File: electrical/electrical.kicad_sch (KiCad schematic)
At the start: 0 parts

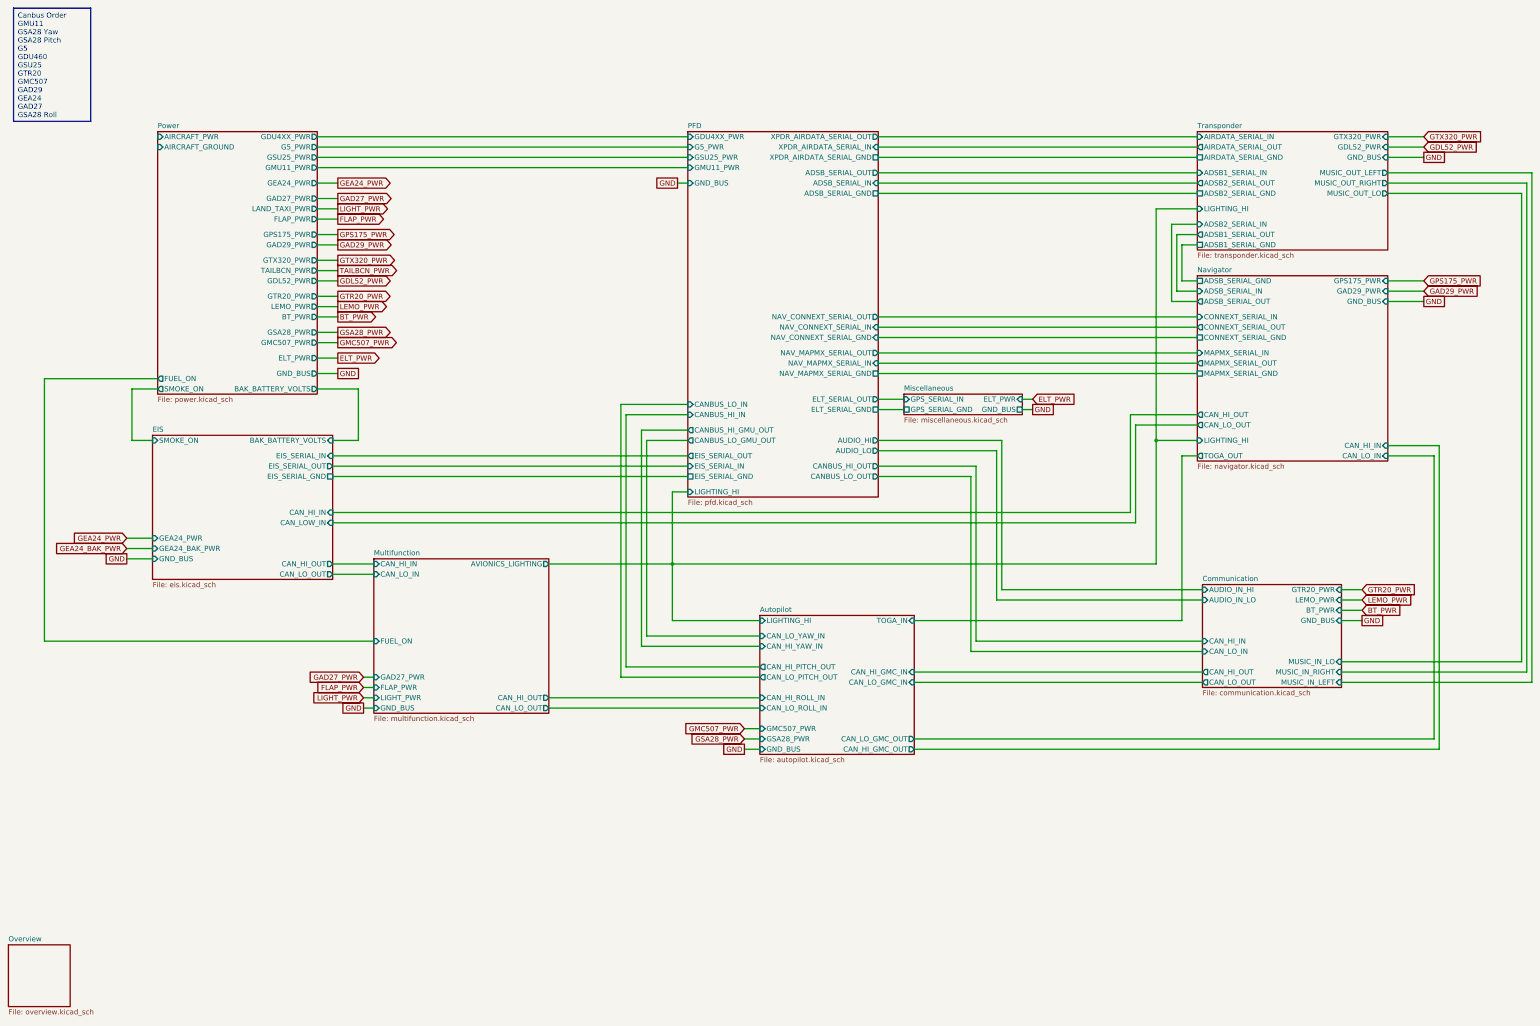
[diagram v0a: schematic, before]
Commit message: Added Altitude Encoder for 320, also added RS232 air data to Transponder in case upgrade to a GTX 327
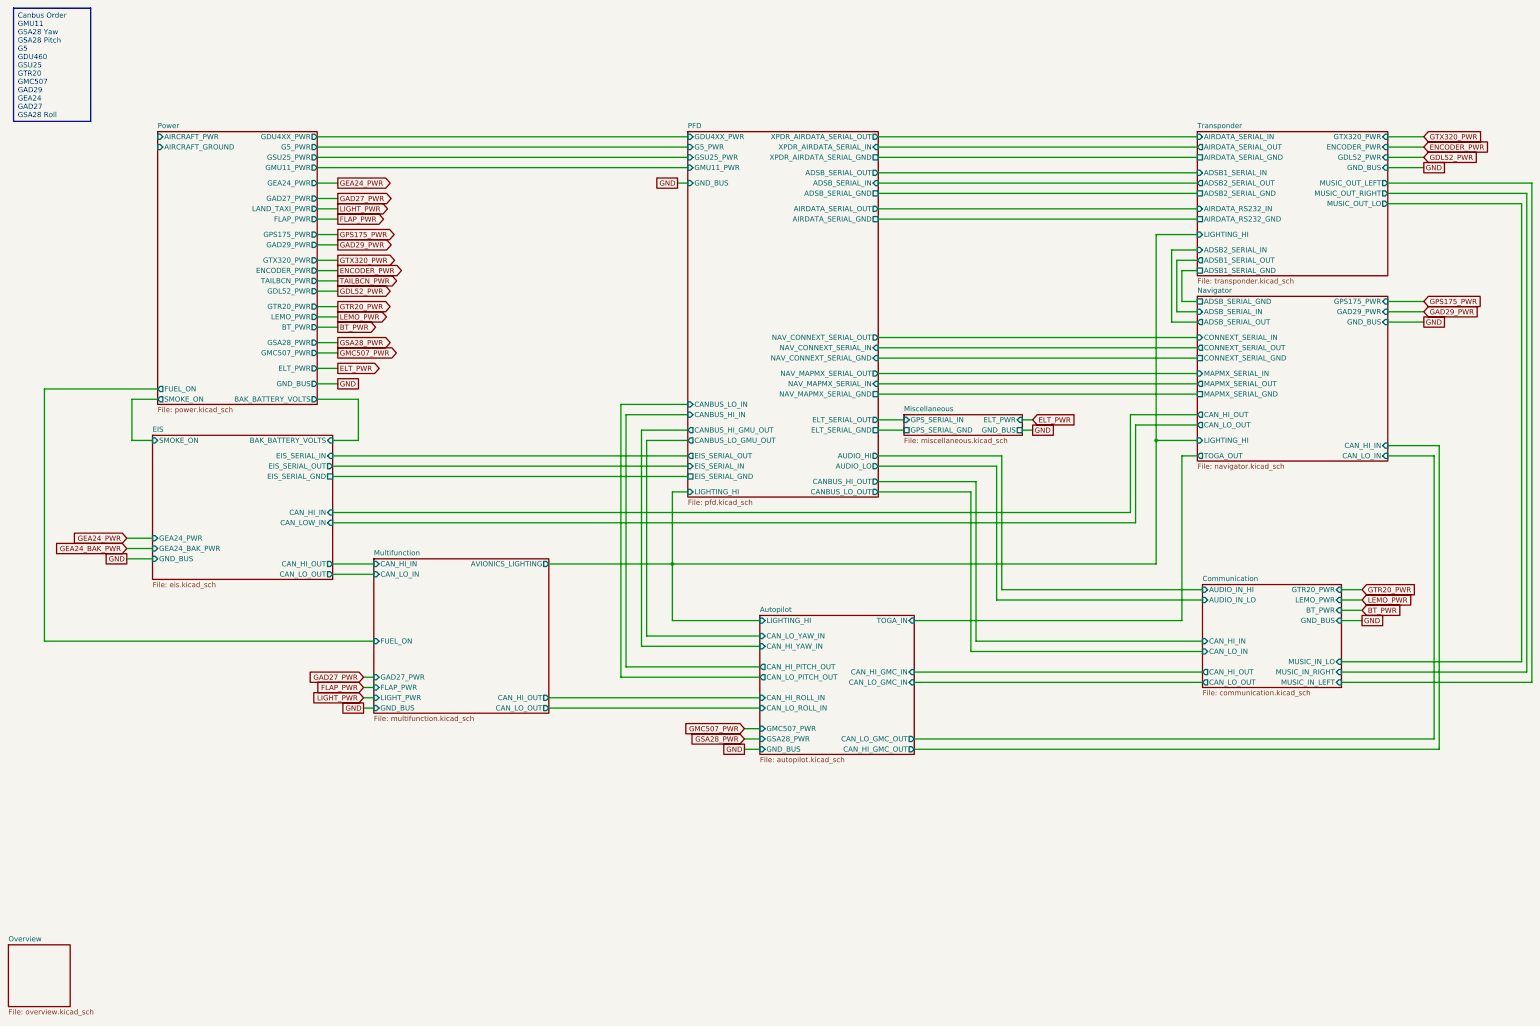
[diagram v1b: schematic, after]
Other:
- sheet PFD ports: added AIRDATA_SERIAL_GND, AIRDATA_SERIAL_OUT; removed none
- sheet Power ports: added ENCODER_PWR; removed none
- sheet Transponder ports: added AIRDATA_RS232_GND, AIRDATA_RS232_IN, ENCODER_PWR; removed none

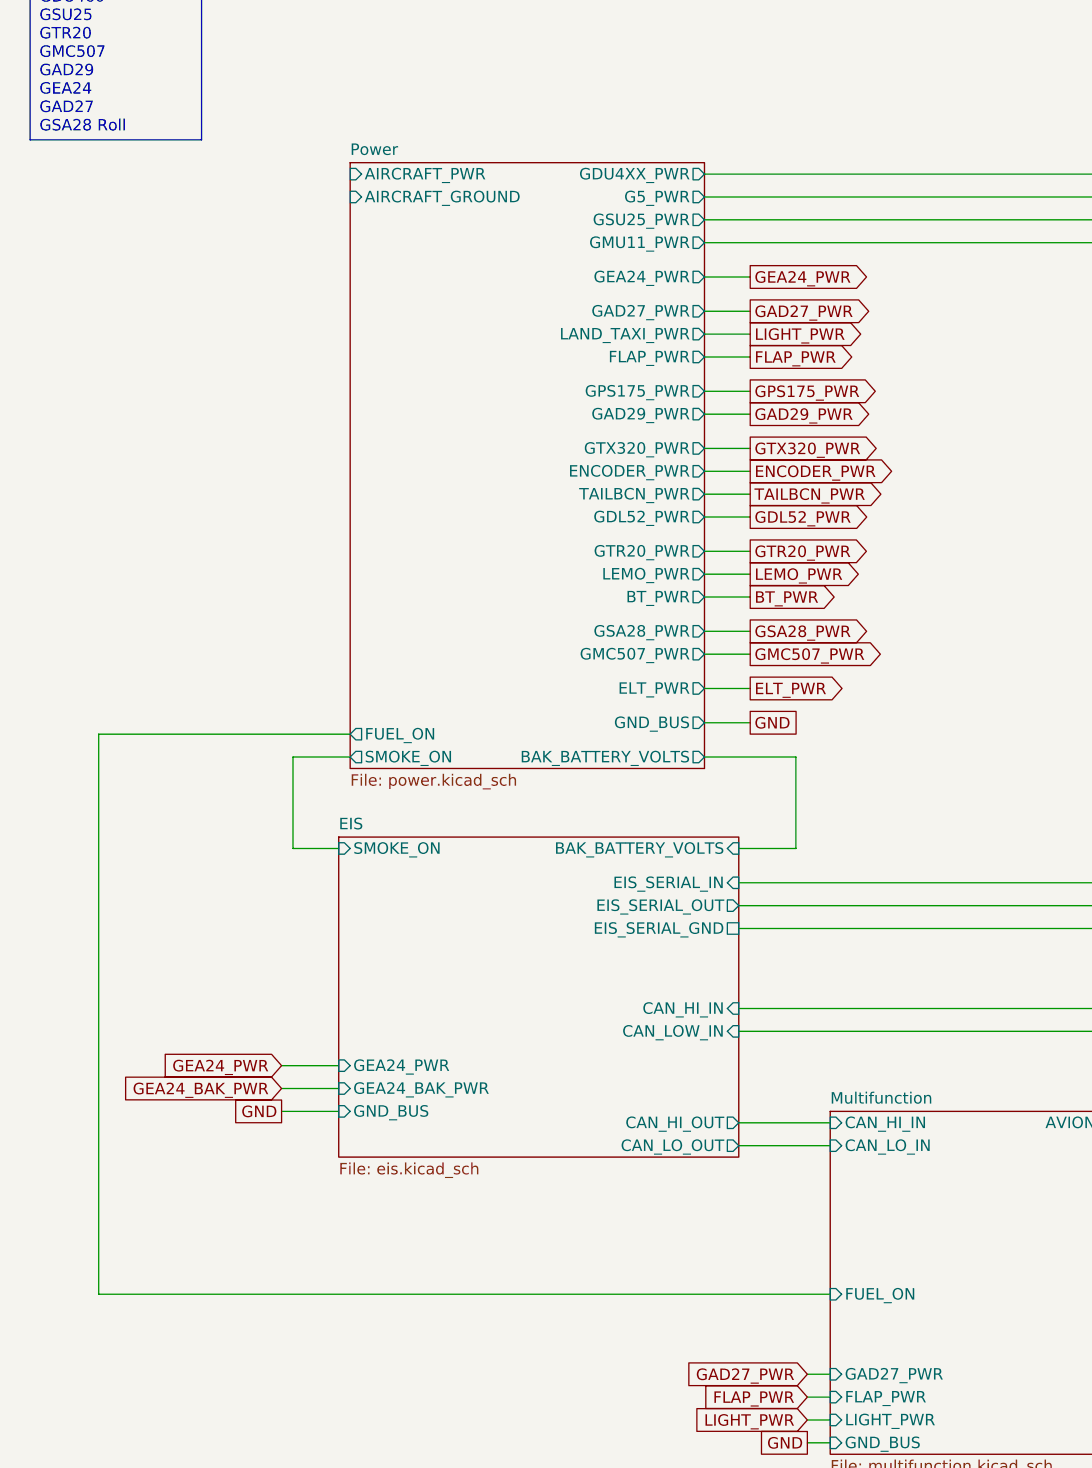
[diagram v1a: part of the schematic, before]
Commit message: Added AV breaker. Added diodes to TOGA. Moved smoke to use roll trim. Changec cabin & panel to use a single fuse.
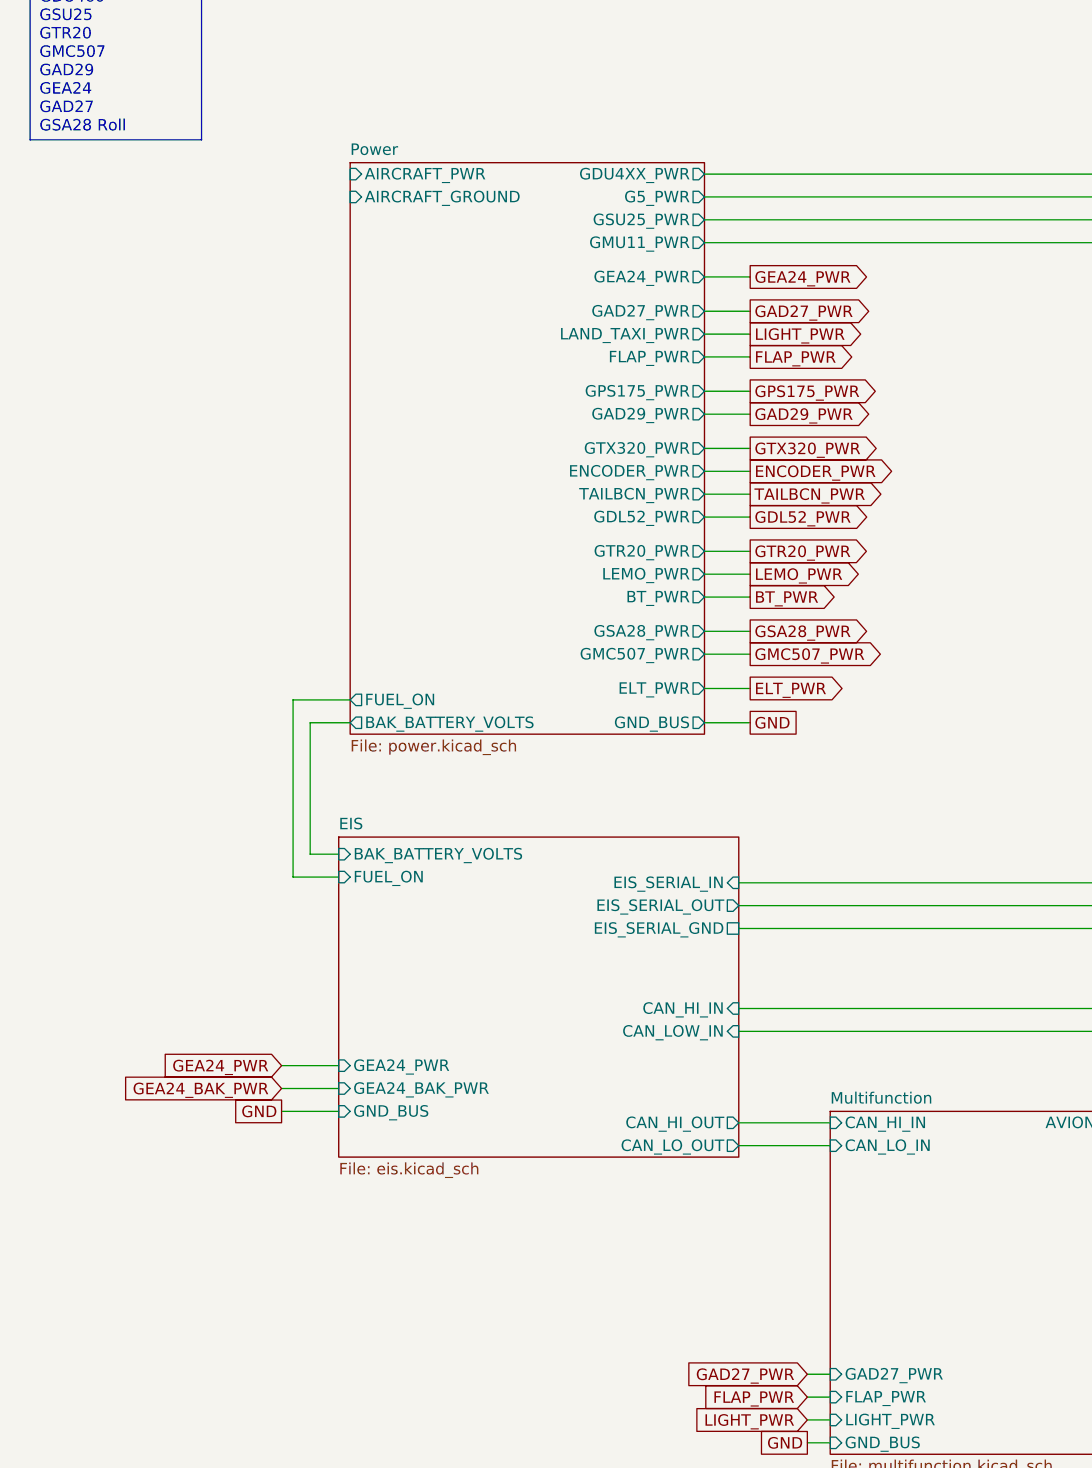
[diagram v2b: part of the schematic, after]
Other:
- sheet EIS ports: added FUEL_ON; removed SMOKE_ON
- sheet Multifunction ports: added none; removed FUEL_ON
- sheet Power ports: added none; removed SMOKE_ON
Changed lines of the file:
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@@
   (title_block
     (title "Electrical Overview")
-    (date "2024-05-07")
-    (rev "1.0.2")
+    (date "2024-05-21")
+    (rev "1.0.3")
     (company "N877RV")
   )
@@
     (stroke (width 0) (type default))
   )
-  (wire (pts (xy 52.07 113.03) (xy 45.72 113.03))
-    (stroke (width 0) (type default))
-  )
   (wire (pts (xy 166.37 114.3) (xy 182.88 114.3))
     (stroke (width 0) (type default))
@@
     (stroke (width 0) (type default))
   )
-  (wire (pts (xy 101.6 113.03) (xy 101.6 123.19))
-    (stroke (width 0) (type default))
-  )
   (wire (pts (xy 259.08 162.56) (xy 309.88 162.56))
     (stroke (width 0) (type default))
   )
+  (wire (pts (xy 52.07 106.68) (xy 45.72 106.68))
+    (stroke (width 0) (type default))
+  )
   (wire (pts (xy 308.61 72.39) (xy 298.45 72.39))
     (stroke (width 0) (type default))
   )
+  (wire (pts (xy 47.625 109.22) (xy 47.625 123.825))
+    (stroke (width 0) (type default))
+  )
   (wire (pts (xy 389.89 62.23) (xy 389.89 180.34))
     (stroke (width 0) (type default))
@@
     (stroke (width 0) (type default))
   )
+  (wire (pts (xy 45.72 126.365) (xy 50.8 126.365))
+    (stroke (width 0) (type default))
+  )
   (wire (pts (xy 355.6 93.98) (xy 364.49 93.98))
     (stroke (width 0) (type default))
@@
     (stroke (width 0) (type default))
   )
+  (wire (pts (xy 45.72 106.68) (xy 45.72 126.365))
+    (stroke (width 0) (type default))
+  )
   (wire (pts (xy 172.72 171.45) (xy 200.66 171.45))
     (stroke (width 0) (type default))
   )
-  (wire (pts (xy 45.72 113.03) (xy 45.72 123.19))
-    (stroke (width 0) (type default))
-  )
   (wire (pts (xy 355.6 88.9) (xy 364.49 88.9))
     (stroke (width 0) (type default))
@@
     (stroke (width 0) (type default))
   )
-  (wire (pts (xy 24.13 172.72) (xy 105.41 172.72))
-    (stroke (width 0) (type default))
-  )
   (wire (pts (xy 229.87 53.34) (xy 308.61 53.34))
     (stroke (width 0) (type default))
@@
     (stroke (width 0) (type default))
   )
-  (wire (pts (xy 91.44 113.03) (xy 101.6 113.03))
-    (stroke (width 0) (type default))
-  )
   (wire (pts (xy 148.59 153.67) (xy 179.07 153.67))
     (stroke (width 0) (type default))
@@
     (stroke (width 0) (type default))
   )
-  (wire (pts (xy 24.13 110.49) (xy 24.13 172.72))
+  (wire (pts (xy 52.07 109.22) (xy 47.625 109.22))
     (stroke (width 0) (type default))
   )
@@
     (stroke (width 0) (type default))
   )
-  (wire (pts (xy 45.72 123.19) (xy 50.8 123.19))
-    (stroke (width 0) (type default))
-  )
   (wire (pts (xy 292.1 140.97) (xy 95.25 140.97))
     (stroke (width 0) (type default))
@@
     (stroke (width 0) (type default))
   )
-  (wire (pts (xy 95.25 123.19) (xy 101.6 123.19))
-    (stroke (width 0) (type default))
-  )
   (wire (pts (xy 308.61 78.74) (xy 303.53 78.74))
     (stroke (width 0) (type default))
@@
     (stroke (width 0) (type default))
   )
+  (wire (pts (xy 47.625 123.825) (xy 50.8 123.825))
+    (stroke (width 0) (type default))
+  )
   (wire (pts (xy 367.03 196.85) (xy 367.03 127))
-    (stroke (width 0) (type default))
-  )
-  (wire (pts (xy 52.07 110.49) (xy 24.13 110.49))
     (stroke (width 0) (type default))
   )
@@
     )
   )
-  (sheet (at 52.07 46.99) (size 39.37 67.31) (fields_autoplaced)
+  (sheet (at 52.07 46.99) (size 39.37 63.5) (fields_autoplaced)
     (stroke (width 0.1524) (type solid))
     (fill (color 0 0 0 0.0000))
@@
       (effects (font (size 1.27 1.27)) (justify left bottom))
     )
-    (property "Sheetfile" "power.kicad_sch" (at 52.07 114.8846 0)
+    (property "Sheetfile" "power.kicad_sch" (at 52.07 111.0746 0)
       (effects (font (size 1.27 1.27)) (justify left top))
     )
@@
       (effects (font (size 1.27 1.27)) (justify right))
     )
-    (pin "BAK_BATTERY_VOLTS" output (at 91.44 113.03 0)
-      (effects (font (size 1.27 1.27)) (justify right))
+    (pin "BAK_BATTERY_VOLTS" output (at 52.07 109.22 180)
+      (effects (font (size 1.27 1.27)) (justify left))
     )
     (pin "GMC507_PWR" output (at 91.44 101.6 0)
@@
       (effects (font (size 1.27 1.27)) (justify right))
     )
-    (pin "SMOKE_ON" output (at 52.07 113.03 180)
-      (effects (font (size 1.27 1.27)) (justify left))
-    )
     (pin "BT_PWR" output (at 91.44 95.25 0)
       (effects (font (size 1.27 1.27)) (justify right))
     )
-    (pin "FUEL_ON" output (at 52.07 110.49 180)
+    (pin "FUEL_ON" output (at 52.07 106.68 180)
       (effects (font (size 1.27 1.27)) (justify left))
     )
@@
       (effects (font (size 1.27 1.27)) (justify right))
     )
-    (pin "FUEL_ON" input (at 105.41 172.72 180)
-      (effects (font (size 1.27 1.27)) (justify left))
-    )
     (instances
       (project "electrical"
@@
       (effects (font (size 1.27 1.27)) (justify right))
     )
-    (pin "BAK_BATTERY_VOLTS" input (at 95.25 123.19 0)
-      (effects (font (size 1.27 1.27)) (justify right))
+    (pin "BAK_BATTERY_VOLTS" input (at 50.8 123.825 180)
+      (effects (font (size 1.27 1.27)) (justify left))
     )
     (pin "EIS_SERIAL_OUT" output (at 95.25 129.54 0)
@@
       (effects (font (size 1.27 1.27)) (justify right))
     )
-    (pin "SMOKE_ON" input (at 50.8 123.19 180)
-      (effects (font (size 1.27 1.27)) (justify left))
-    )
+    (pin "FUEL_ON" input (at 50.8 126.365 180)
+      (effects (font (size 1.27 1.27)) (justify left))
+    )
